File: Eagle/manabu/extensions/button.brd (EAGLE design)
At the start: 5 parts

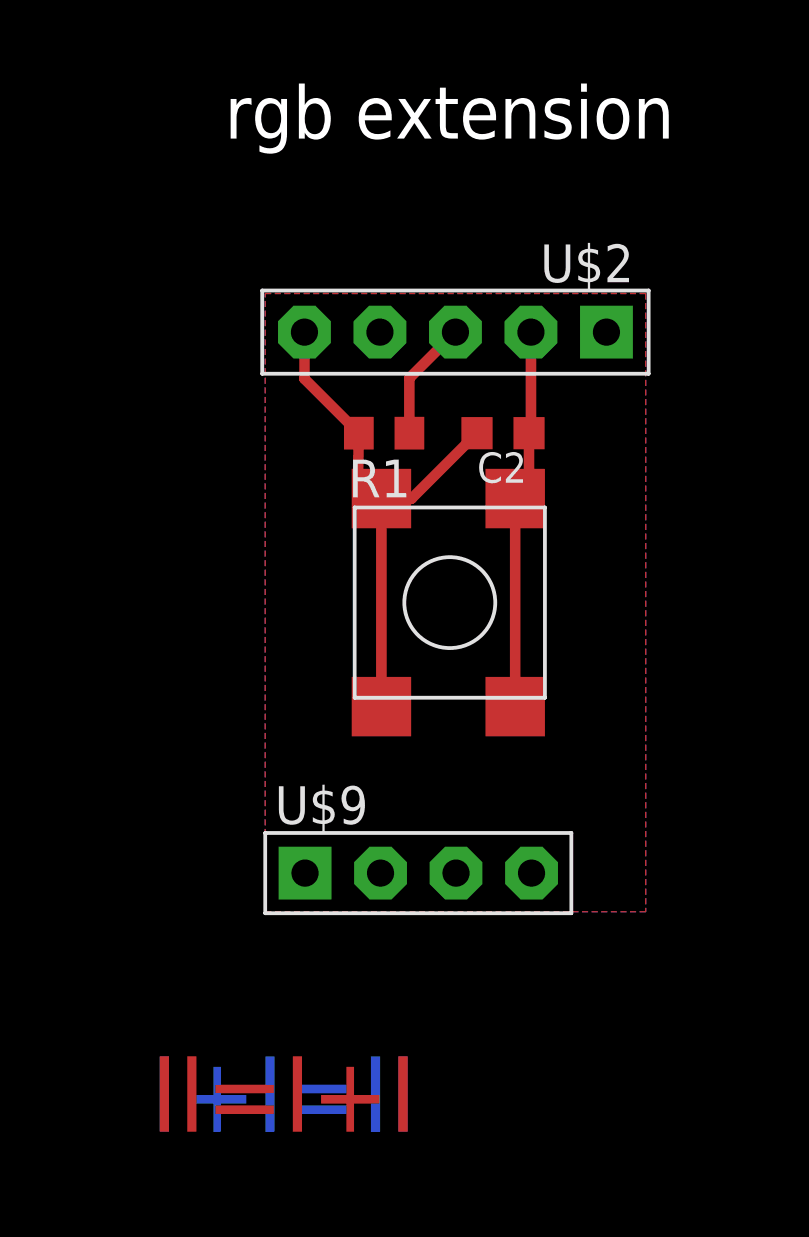
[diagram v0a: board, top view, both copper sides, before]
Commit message: added button 12x12 and then used in button extension
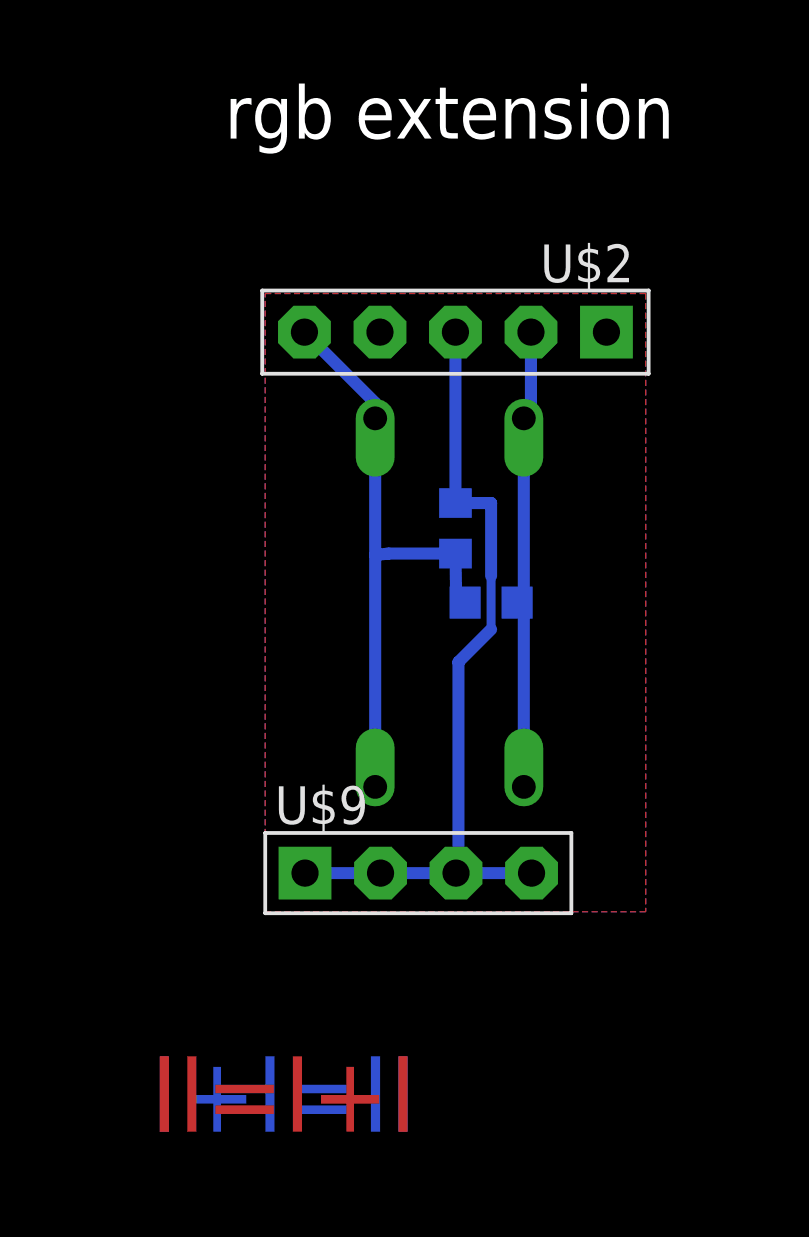
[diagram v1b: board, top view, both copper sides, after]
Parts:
- U$1: value BUTTON_6.3X6.3 -> BUTTON_7X7; device !stavebnice03:BUTTON_6.2X6.2 -> !stavebnice03:BUTTON_7X7
- moved C2 5.71 mm to (11.9, 10.5), flipped to the bottom, turned to 0 degrees
- moved R1 4.00 mm to (10.7, 13.0), flipped to the bottom, turned to 270 degrees
- turned U$1 to 0 degrees
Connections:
- net AA: now also U$1.B1, U$1.B2; no longer U$1.P$2, U$1.P$4
- net VCC: now also U$1.A1, U$1.A2; no longer U$1.P$1, U$1.P$3
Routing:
- net GND: track 4.04 -> 27.5 mm
- net VCC: track 12.8 -> 15.6 mm
- net AA: track 18.5 -> 20.8 mm
